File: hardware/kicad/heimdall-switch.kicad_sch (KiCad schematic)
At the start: 42 parts, among them J1 SWD (ARM 10-pin), J2 LOAD_OUT, J3 BATT_IN, J4 B3B-XH-A, Q1 AO3400A, Q2 BSS84, Q3 AO4407A, Q4 AO4407A, Q5 AO3400A, Q6 BSS84, SW1 KSC641J, U1 BT832, U2 TPS629206, Y1 32.768kHz

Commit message: Annotate main schematic and assign all footprints
- Descriptive references (R_PD1, C_SS, D_Z, ...) renamed to R1-R16,
  C3-C8, D1-D2; old names kept in a hidden "Function" field and mapped
  in hardware.md
- Footprints on every part (KiCad stock, plus project-local
  Fanstel_BT832 drawn from the datasheet with an antenna keep-out)
- Q3/Q4 use a new AO4407A symbol: generic P-FET drawing with SO-8 pin
  numbers (G=4, S=1-3, D=5-8 stacked), so no wiring moved

ERC 0/0, netlist identical net-for-net after mapping, every pin has a
matching footprint pad.

Co-Authored-By: Claude Opus 5.5 <noreply@anthropic.com>
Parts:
- C1, C2: footprint (none) -> Capacitor_SMD:C_0603_1608Metric
- C3: renamed from C_IN; footprint (none) -> Capacitor_SMD:C_1206_3216Metric; Function (none) -> C_IN
- C4: renamed from C_OUT; footprint (none) -> Capacitor_SMD:C_0805_2012Metric; Function (none) -> C_OUT
- C5: renamed from C_VDD1; footprint (none) -> Capacitor_SMD:C_0603_1608Metric; Function (none) -> C_VDD1
- C6: renamed from C_VDD2; footprint (none) -> Capacitor_SMD:C_0603_1608Metric; Function (none) -> C_VDD2
- C7: renamed from C_SS; footprint (none) -> Capacitor_SMD:C_0805_2012Metric; Function (none) -> C_SS
- C8: renamed from C_FB; footprint (none) -> Capacitor_SMD:C_0603_1608Metric; Function (none) -> C_FB
- D1: renamed from D_Z2; footprint (none) -> Diode_SMD:D_SOD-123; Function (none) -> D_Z2
- D2: renamed from D_Z; footprint (none) -> Diode_SMD:D_SOD-123; Function (none) -> D_Z
- J1: footprint (none) -> Connector_PinHeader_1.27mm:PinHeader_2x05_P1.27mm_Vertical_SMD
- J2, J3: footprint (none) -> Connector_Wire:SolderWire-0.75sqmm_1x02_P4.8mm_D1.25mm_OD2.3mm_Relief
- J4: footprint (none) -> Connector_JST:JST_XH_B3B-XH-A_1x03_P2.50mm_Vertical
- L1: footprint (none) -> Inductor_SMD:L_1008_2520Metric
- LED1: footprint (none) -> LED_THT:LED_D3.0mm
- Q1, Q2, Q5, Q6: footprint (none) -> Package_TO_SOT_SMD:SOT-23
- Q3, Q4: footprint (none) -> Package_SO:SOIC-8_3.9x4.9mm_P1.27mm; symbol Transistor_FET:Q_PMOS_GSD -> heimdall-switch:AO4407A
- R1: renamed from R_REV; footprint (none) -> Resistor_SMD:R_0603_1608Metric; Function (none) -> R_REV
- R10: renamed from R_PD2; footprint (none) -> Resistor_SMD:R_0603_1608Metric; Function (none) -> R_PD2
- R11: renamed from R_FB_TOP; footprint (none) -> Resistor_SMD:R_0603_1608Metric; Function (none) -> R_FB_TOP
- R12: renamed from R_FB_BOT; footprint (none) -> Resistor_SMD:R_0603_1608Metric; Function (none) -> R_FB_BOT
- R13: renamed from R_Q6_PU; footprint (none) -> Resistor_SMD:R_0603_1608Metric; Function (none) -> R_Q6_PU
- R14: renamed from R_LED; footprint (none) -> Resistor_SMD:R_1206_3216Metric; Function (none) -> R_LED
- R15: renamed from R_LED_PD; footprint (none) -> Resistor_SMD:R_0603_1608Metric; Function (none) -> R_LED_PD
- R16: renamed from R_BTN; footprint (none) -> Resistor_SMD:R_0603_1608Metric; Function (none) -> R_BTN
- R2: renamed from R_IN; footprint (none) -> Resistor_SMD:R_0603_1608Metric; Function (none) -> R_IN
- R3: renamed from R_MODE; footprint (none) -> Resistor_SMD:R_0603_1608Metric; Function (none) -> R_MODE
- R4: renamed from R_RST; footprint (none) -> Resistor_SMD:R_0603_1608Metric; Function (none) -> R_RST
- R5: renamed from R_G1; footprint (none) -> Resistor_SMD:R_0603_1608Metric; Function (none) -> R_G1
- R6: renamed from R_OFF_PD; footprint (none) -> Resistor_SMD:R_0603_1608Metric; Function (none) -> R_OFF_PD
- R7: renamed from R_CLAMP_PU; footprint (none) -> Resistor_SMD:R_0603_1608Metric; Function (none) -> R_CLAMP_PU
- R8: renamed from R_LIM; footprint (none) -> Resistor_SMD:R_0603_1608Metric; Function (none) -> R_LIM
- R9: renamed from R_PD1; footprint (none) -> Resistor_SMD:R_0603_1608Metric; Function (none) -> R_PD1
- SW1: footprint (none) -> Button_Switch_SMD:SW_Push_1P1T_NO_CK_KSC6xxJ
- U1: footprint (none) -> heimdall-switch:Fanstel_BT832
- U2: footprint (none) -> Package_TO_SOT_SMD:SOT-583-8
- Y1: footprint (none) -> Crystal:Crystal_SMD_3215-2Pin_3.2x1.5mm
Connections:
- net BATT+: now also Q4.5 (D), Q4.6 (D), Q4.7 (D), Q4.8 (D); no longer Q4.3 (D)
- net LOAD_OUT: now also Q3.5 (D), Q3.6 (D), Q3.7 (D), Q3.8 (D); no longer Q3.3 (D)
- net Q3_GATE: now also Q3.4 (G); no longer Q3.1 (G)
- net VBAT: now also Q3.1 (S), Q3.3 (S), Q4.1 (S), Q4.3 (S)
- net at D1.2 (A), R1.1: now also Q4.4 (G); no longer Q4.1 (G)

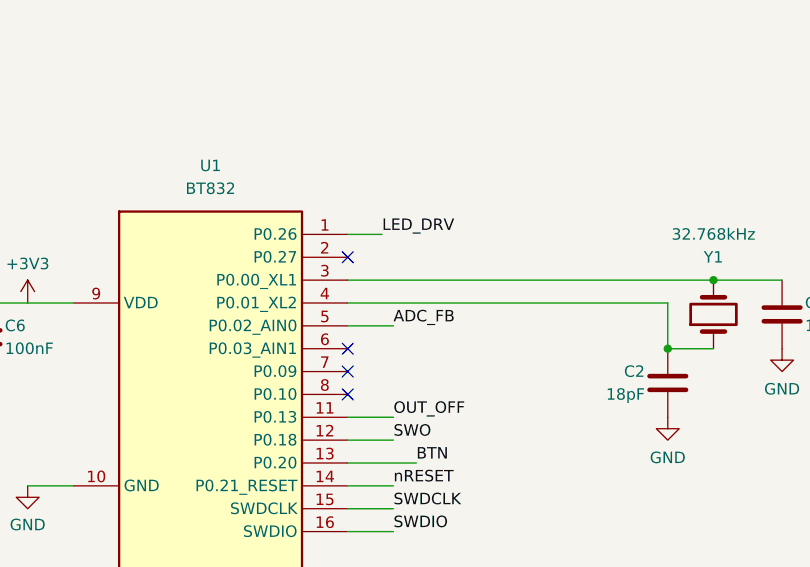
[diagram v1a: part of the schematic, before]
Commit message: Main PCB: placement iteration 1 (unrouted); LED drive to P0.03
Long, slim 95.8 x 23 mm board: battery/load wire pads with strain relief
at the left end, Q4/Q3 right behind them on a short VBAT bar, gate
networks and regulator in the middle, BT832 at the right end with its
antenna overhanging the edge. Generated with place_pcb.py (KiCad python)
from the netlist; DRC: no courtyard overlaps, full schematic parity.

LED_DRV moved from P0.26 (pin 1) to P0.03 (pin 6) so the module's top
pin row exits left without crossing the crystal.

Co-Authored-By: Claude Opus 5.5 <noreply@anthropic.com>
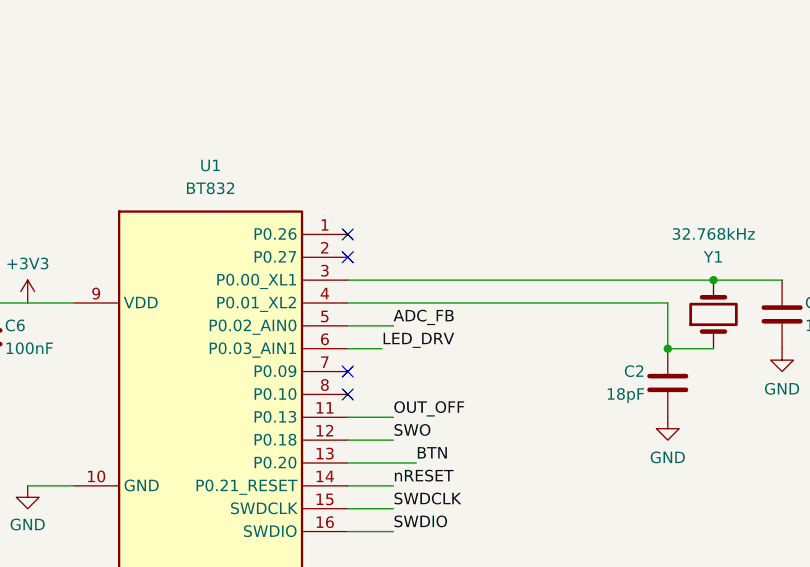
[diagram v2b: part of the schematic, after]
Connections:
- net LED_DRV: now also U1.6 (P0.03_AIN1); no longer U1.1 (P0.26)
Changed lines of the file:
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@@
-	)
-	(no_connect
-		(at 195.58 83.82)
 	)
 	(no_connect
@@
 	)
 	(no_connect
+		(at 195.58 71.12)
+	)
+	(no_connect
 		(at 195.58 88.9)
 	)
@@
 	(wire
 		(pts
-			(xy 195.58 71.12) (xy 199.39 71.12)
-		)
-		(stroke
-			(width 0)
-			(type default)
-		)
-	)
-	(wire
-		(pts
 			(xy 294.64 127) (xy 292.1 127)
 		)
@@
 		(pts
 			(xy 55.88 149.86) (xy 55.88 139.7)
+		)
+		(stroke
+			(width 0)
+			(type default)
+		)
+	)
+	(wire
+		(pts
+			(xy 195.58 83.82) (xy 199.39 83.82)
 		)
 		(stroke
@@
 		)
 	)
+	(label "LED_DRV"
+		(at 199.39 83.82 0)
+		(effects
+			(font
+				(size 1.27 1.27)
+			)
+			(justify left bottom)
+		)
+	)
 	(label "OUT_OFF"
 		(at 200.66 91.44 0)
@@
 		(effects
 			(font
-				(size 1.27 1.27)
-			)
-			(justify left bottom)
-		)
-	)
-	(label "LED_DRV"
-		(at 199.39 71.12 0)
-		(effects
-			(font

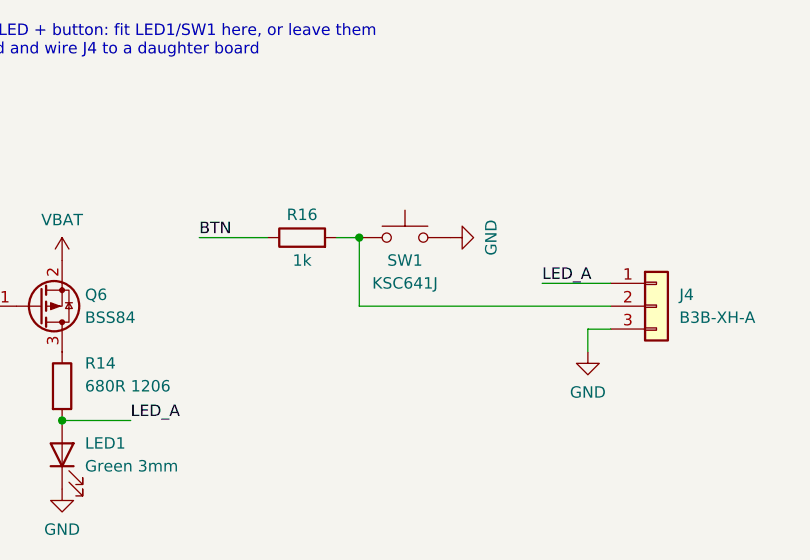
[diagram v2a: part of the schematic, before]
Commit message: Main board SW1: small C&K PTS810 (4.2x3.2mm), placed next to LED1
The sealed KSC641J stays on the daughter board, which sits outside the
hull; the on-board button is inside, so a small unsealed part is fine.

Co-Authored-By: Claude Opus 5.5 <noreply@anthropic.com>
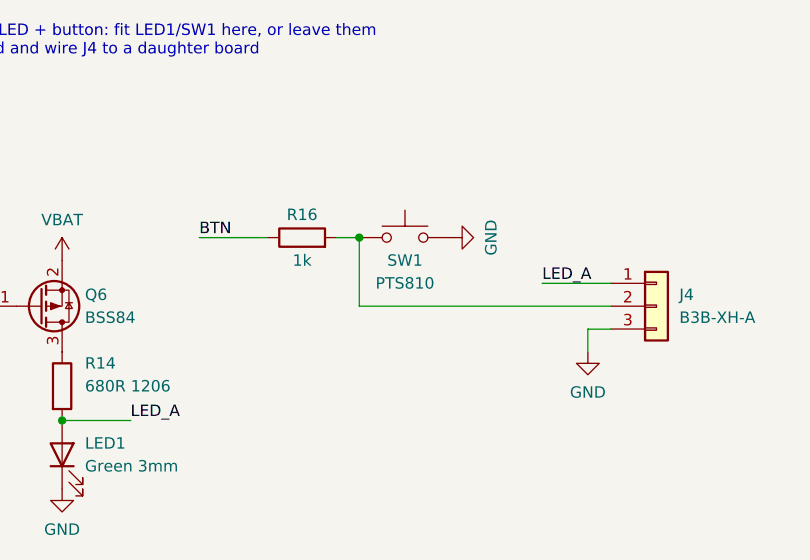
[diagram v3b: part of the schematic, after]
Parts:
- SW1: value KSC641J -> PTS810; footprint Button_Switch_SMD:SW_Push_1P1T_NO_CK_KSC6xxJ -> Button_Switch_SMD:SW_SPST_PTS810; LCSC C226344 -> C116501
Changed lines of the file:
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@@
 			)
 		)
-		(property "Value" "KSC641J"
+		(property "Value" "PTS810"
 			(at 275.59 179.07 0)
 			(show_name no)
@@
 			)
 		)
-		(property "Footprint" "Button_Switch_SMD:SW_Push_1P1T_NO_CK_KSC6xxJ"
+		(property "Footprint" "Button_Switch_SMD:SW_SPST_PTS810"
 			(at 275.59 173.99 0)
 			(hide yes)
@@
 			)
 		)
-		(property "LCSC" "C226344"
+		(property "LCSC" "C116501"
 			(at 275.59 173.99 0)
 			(hide yes)

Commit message: BOM: swap out-of-stock C3 (C89632) and R4 (C98220)
C13585 and C25804 are out of stock at LCSC. C3 becomes CL31B106KBHNNNE
(10uF 50V X7R 1206, less DC-bias loss than the X5R), R4 the Yageo
RC0603FR-0710KL 10k.

Co-Authored-By: Claude Opus 5.5 <noreply@anthropic.com>
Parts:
- C3: LCSC C13585 -> C89632
- R4: LCSC C25804 -> C98220
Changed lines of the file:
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@@
 			)
 		)
-		(property "LCSC" "C25804"
+		(property "LCSC" "C98220"
 			(at 274.32 100.33 0)
 			(hide yes)
@@
 			)
 		)
-		(property "LCSC" "C13585"
+		(property "LCSC" "C89632"
 			(at 45.72 52.07 0)
 			(hide yes)

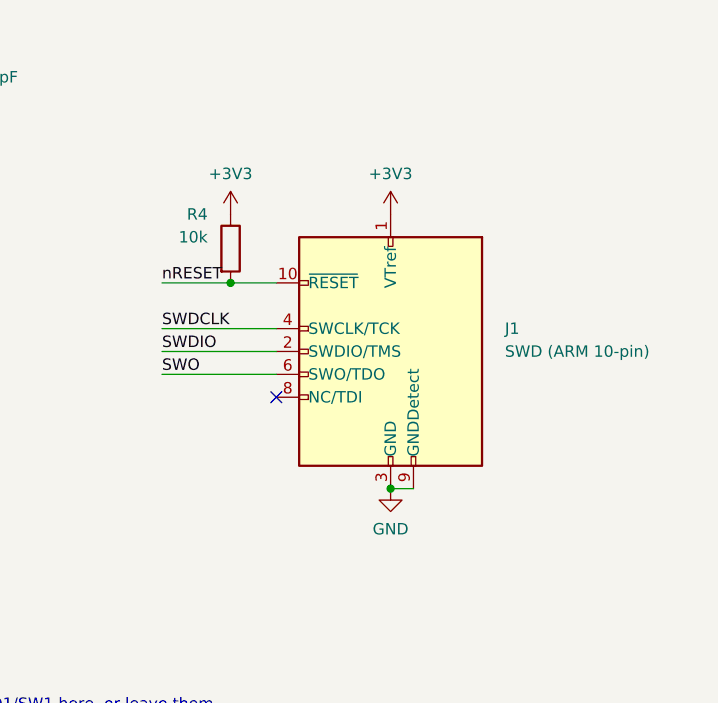
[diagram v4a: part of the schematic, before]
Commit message: J1: Tag-Connect TC2030-NL in place of the 2x5 SWD header
The Samtec FTSH-105 cost $1.46/board for a connector used once per
board (to flash the DFU bootloader). The TC2030-NL footprint is pads
plus three locating holes, no part; the TC2030-CTX-NL cable ends in the
same ARM 10-pin socket the probes use. No-legs variant so nothing goes
through to the populated bottom side.

Schematic: J1 symbol swapped to Conn_ARM_SWD_TagConnect_TC2030-NL,
labels rewired, excluded from BOM. PCB: footprint in J1's old spot,
SWD nets re-routed with everything else locked (rotation 0 of four
tried), +3V3 to pad 1 hand-routed. ERC/DRC clean, full parity.

Co-Authored-By: Claude Opus 5.5 <noreply@anthropic.com>
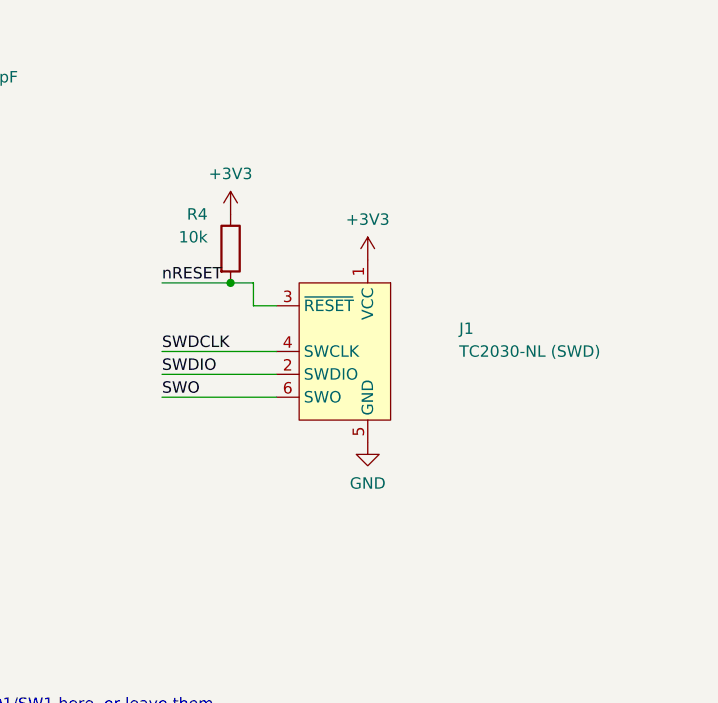
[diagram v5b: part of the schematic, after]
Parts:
- J1: value SWD (ARM 10-pin) -> TC2030-NL (SWD); footprint Connector_PinHeader_1.27mm:PinHeader_2x05_P1.27mm_Vertical_SMD -> Connector:Tag-Connect_TC2030-IDC-NL_2x03_P1.27mm_Vertical; symbol Connector:Conn_ARM_JTAG_SWD_10 -> Connector:Conn_ARM_SWD_TagConnect_TC2030-NL; LCSC C5155080 -> (none); now left out of the parts list
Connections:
- net GND: no longer J1.3 (GND), J1.9 (GNDDetect)
- net nRESET: now also J1.3 (~{RESET}); no longer J1.10 (~{RESET})
- no-connect marks 7 -> 6
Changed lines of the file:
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@@
 	)
 	(junction
-		(at 292.1 127)
-		(diameter 0)
-		(color 0 0 0 0)
-	)
-	(junction
 		(at 71.12 48.26)
 		(diameter 0)
@@
 	)
 	(no_connect
-		(at 279.4 116.84)
-	)
-	(no_connect
 		(at 195.58 71.12)
 	)
@@
 	(wire
 		(pts
-			(xy 294.64 127) (xy 292.1 127)
-		)
-		(stroke
-			(width 0)
-			(type default)
-		)
-	)
-	(wire
-		(pts
 			(xy 27.94 167.64) (xy 34.29 167.64)
 		)
@@
 	(wire
 		(pts
-			(xy 266.7 109.22) (xy 279.4 109.22)
+			(xy 266.7 111.76) (xy 279.4 111.76)
 		)
 		(stroke
@@
 	(wire
 		(pts
-			(xy 266.7 111.76) (xy 279.4 111.76)
+			(xy 266.7 114.3) (xy 279.4 114.3)
 		)
 		(stroke
@@
 	(wire
 		(pts
-			(xy 274.32 104.14) (xy 279.4 104.14)
+			(xy 274.32 104.14) (xy 276.86 104.14)
+		)
+		(stroke
+			(width 0)
+			(type default)
+		)
+	)
+	(wire
+		(pts
+			(xy 276.86 104.14) (xy 276.86 106.68)
+		)
+		(stroke
+			(width 0)
+			(type default)
+		)
+	)
+	(wire
+		(pts
+			(xy 276.86 106.68) (xy 279.4 106.68)
 		)
 		(stroke
@@
 	(wire
 		(pts
-			(xy 266.7 114.3) (xy 279.4 114.3)
+			(xy 266.7 116.84) (xy 279.4 116.84)
 		)
 		(stroke
@@
 	)
 	(label "SWO"
-		(at 266.7 114.3 0)
+		(at 266.7 116.84 0)
 		(effects
 			(font
@@
 	)
 	(label "SWDIO"
-		(at 266.7 111.76 0)
+		(at 266.7 114.3 0)
 		(effects
 			(font
@@
 	)
 	(label "SWDCLK"
-		(at 266.7 109.22 0)
+		(at 266.7 111.76 0)
 		(effects
 			(font
@@
 	(symbol
 		(lib_id "power:GND")
-		(at 292.1 127 0)
+		(at 289.56 121.92 0)
 		(unit 1)
 		(body_style 1)
@@
 		(dnp no)
 		(property "Reference" "#PWR112"
-			(at 292.1 127 0)
+			(at 289.56 121.92 0)
 			(hide yes)
 			(show_name no)
@@
 		)
 		(property "Value" "GND"
-			(at 292.1 131.5 0)
+			(at 289.56 126.42 0)
 			(show_name no)
 			(do_not_autoplace no)
@@
 		)
 		(property "Footprint" ""
-			(at 292.1 127 0)
+			(at 289.56 121.92 0)
 			(hide yes)
 			(show_name no)
@@
 		)
 		(property "Datasheet" ""
-			(at 292.1 127 0)
+			(at 289.56 121.92 0)
 			(hide yes)
 			(show_name no)
@@
 		)
 		(property "Description" ""
-			(at 292.1 127 0)
+			(at 289.56 121.92 0)
 			(show_name no)
 			(do_not_autoplace no)
@@
 	(symbol
 		(lib_id "power:+3V3")
-		(at 292.1 96.52 0)
+		(at 289.56 101.6 0)
 		(unit 1)
 		(body_style 1)
@@
 		(dnp no)
 		(property "Reference" "#PWR111"
-			(at 292.1 96.52 0)
+			(at 289.56 101.6 0)
 			(hide yes)
 			(show_name no)
@@
 		)
 		(property "Value" "+3V3"
-			(at 292.1 92.02 0)
+			(at 289.56 97.1 0)
 			(show_name no)
 			(do_not_autoplace no)
@@
 		)
 		(property "Footprint" ""
-			(at 292.1 96.52 0)
+			(at 289.56 101.6 0)
 			(hide yes)
 			(show_name no)
@@
 		)
 		(property "Datasheet" ""
-			(at 292.1 96.52 0)
+			(at 289.56 101.6 0)
 			(hide yes)
 			(show_name no)
@@
 		)
 		(property "Description" ""
-			(at 292.1 96.52 0)
+			(at 289.56 101.6 0)
 			(show_name no)
 			(do_not_autoplace no)
@@
 	)
 	(symbol
-		(lib_id "Connector:Conn_ARM_JTAG_SWD_10")
-		(at 292.1 111.76 0)
+		(lib_id "Connector:Conn_ARM_SWD_TagConnect_TC2030-NL")
+		(at 287.02 111.76 0)
 		(mirror y)
 		(unit 1)
 		(body_style 1)
 		(exclude_from_sim no)
-		(in_bom yes)
+		(in_bom no)
 		(on_board yes)
 		(in_pos_files yes)
 		(dnp no)
 		(property "Reference" "J1"
-			(at 304.8 109.22 0)
+			(at 299.72 109.22 0)
 			(show_name no)
 			(do_not_autoplace no)
@@
 			)
 		)
-		(property "Value" "SWD (ARM 10-pin)"
-			(at 304.8 111.76 0)
+		(property "Value" "TC2030-NL (SWD)"
+			(at 299.72 111.76 0)
 			(show_name no)
 			(do_not_autoplace no)
@@
 			)
 		)
-		(property "Footprint" "Connector_PinHeader_1.27mm:PinHeader_2x05_P1.27mm_Vertical_SMD"
-			(at 292.1 111.76 0)
+		(property "Footprint" "Connector:Tag-Connect_TC2030-IDC-NL_2x03_P1.27mm_Vertical"
+			(at 287.02 111.76 0)
 			(hide yes)
 			(show_name no)
@@
 			)
 		)
-		(property "Datasheet" ""
-			(at 292.1 111.76 0)
+		(property "Datasheet" "https://www.tag-connect.com/wp-content/uploads/bsk-pdf-manager/TC2030-CTX_1.pdf"
+			(at 287.02 111.76 0)
 			(hide yes)
 			(show_name no)
@@
 		)
 		(property "Description" ""
-			(at 292.1 111.76 0)
+			(at 287.02 111.76 0)
 			(show_name no)
 			(do_not_autoplace no)
@@
 			)
 		)
-		(property "LCSC" "C5155080"
-			(at 292.1 111.76 0)
+		(property "LCSC" ""
+			(at 287.02 111.76 0)
 			(hide yes)
 			(show_name no)
@@
 		(pin "6"
 		)
-		(pin "7"
-		)
-		(pin "8"
-		)
-		(pin "9"
-		)
-		(pin "10"
-		)
 		(instances
